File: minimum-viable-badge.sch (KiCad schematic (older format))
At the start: 33 parts, among them J101 EDGE_CONNECTOR, P101 USB, P102 BATTERY, P103 POT_LONG, P104 BUTTON_A, P105 BUTTON_B, P106 POT_SHORT, P107 MECH, P108 MECH, P109 MECH, Q101 S8050, Q102 S8050, SW101 PRGM, SW102 RESET, U101 ESP32-WROOM, U102 CP2102

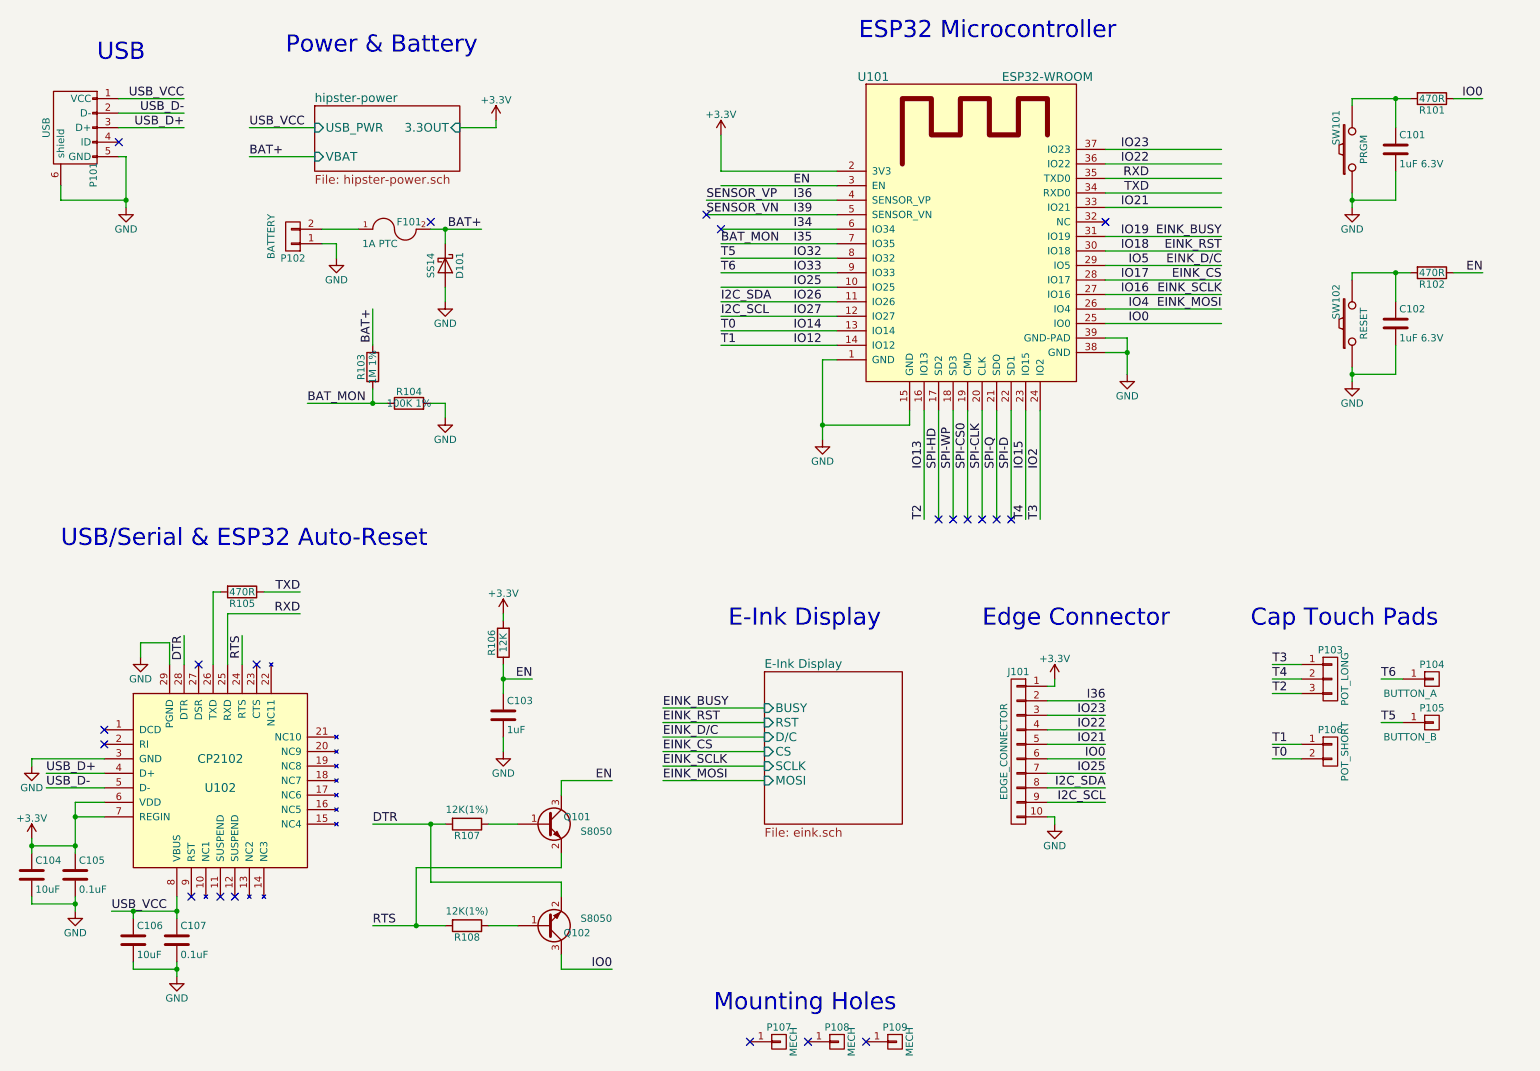
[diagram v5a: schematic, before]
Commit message: Add WS2812Bs for Blinkenlights
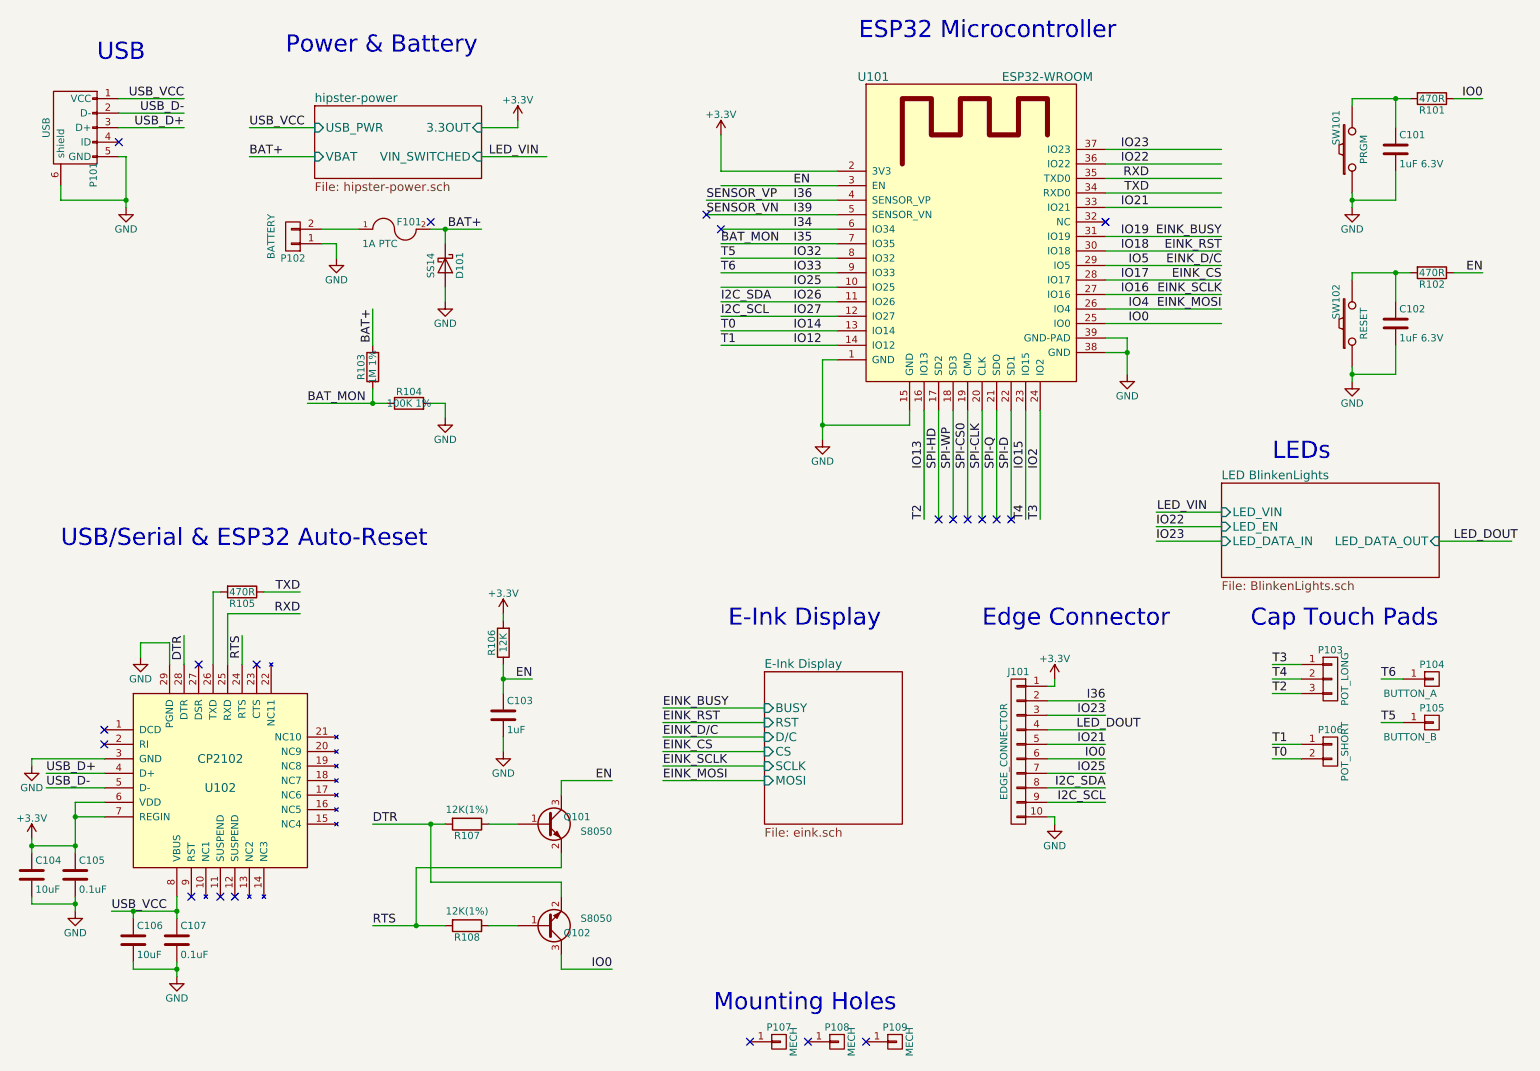
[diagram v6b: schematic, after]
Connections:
- net labels added: LED_DOUT, LED_VIN
- wire segments 149 -> 154
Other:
- note added: "LEDs"
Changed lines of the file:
@@
 $Descr A4 11693 8268
 encoding utf-8
-Sheet 1 3
+Sheet 1 4
 Title ""
 Date ""
@@
 BAT+
 $Sheet
-S 2800 1200 1000 450
+S 2800 1200 1150 500
 U 592826E7
 F0 "hipster-power" 60
@@
 F2 "USB_PWR" I L 2800 1350 60
 F3 "VBAT" I L 2800 1550 60
-F4 "3.3OUT" I R 3800 1350 60
+F4 "3.3OUT" I R 3950 1350 60
+F5 "VIN_SWITCHED" I R 3950 1550 60
 $EndSheet
 $Comp
 L +3.3V #PWR016
 U 1 1 59288975
-P 4050 1300
-F 0 "#PWR016" H 4050 1150 50  0001 C CNN
-F 1 "+3.3V" H 4050 1440 50  0000 C CNN
-F 2 "" H 4050 1300 50  0000 C CNN
-F 3 "" H 4050 1300 50  0000 C CNN
-	1    4050 1300
+P 4200 1300
+F 0 "#PWR016" H 4200 1150 50  0001 C CNN
+F 1 "+3.3V" H 4200 1440 50  0000 C CNN
+F 2 "" H 4200 1300 50  0000 C CNN
+F 3 "" H 4200 1300 50  0000 C CNN
+	1    4200 1300
 	1    0    0    -1
 $EndComp
@@
 Connection ~ 3700 2050
 Wire Wire Line
-	3800 1350 4050 1350
-Wire Wire Line
-	4050 1350 4050 1300
+	3950 1350 4200 1350
+Wire Wire Line
+	4200 1350 4200 1300
 Wire Wire Line
 	2800 1550 2350 1550
@@
 Text Label 8250 5700 2    60   ~ 0
 IO0
-Text Label 8250 5500 2    60   ~ 0
-IO22
-Text Label 8250 5400 2    60   ~ 0
-IO23
 Text Label 8550 1900 2    60   ~ 0
 IO21
 NoConn ~ 5500 1950
 NoConn ~ 5600 2050
+$Sheet
+S 9050 3800 1500 650
+U 59C74472
+F0 "LED BlinkenLights" 60
+F1 "BlinkenLights.sch" 60
+F2 "LED_DATA_IN" I L 9050 4200 60
+F3 "LED_EN" I L 9050 4100 60
+F4 "LED_VIN" I L 9050 4000 60
+F5 "LED_DATA_OUT" I R 10550 4200 60
+$EndSheet
+Text Notes 9400 3650 0    118  ~ 0
+LEDs
+Wire Wire Line
+	10550 4200 11050 4200
+Text Label 10650 4200 0    60   ~ 0
+LED_DOUT
+Text Label 8050 5500 0    60   ~ 0
+LED_DOUT
+Wire Wire Line
+	3950 1550 4400 1550
+Text Label 4000 1550 0    60   ~ 0
+LED_VIN
+Text Label 8950 4000 2    60   ~ 0
+LED_VIN
+Wire Wire Line
+	9050 4000 8600 4000
+Wire Wire Line
+	9050 4100 8600 4100
+Wire Wire Line
+	9050 4200 8600 4200
+Text Label 8600 4100 0    60   ~ 0
+IO22
+Text Label 8600 4200 0    60   ~ 0
+IO23
+Text Label 8250 5400 2    60   ~ 0
+IO23
 $EndSCHEMATC

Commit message: Route LEDs, make edge connector one sided with mounting slots
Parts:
- J101: footprint libs:Edge_Connector_1x10_Pitch2.54mm -> libs:Edge_Connector_S20-2.54-5_bottomsideonly
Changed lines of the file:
@@
 F 0 "J101" H 7650 6200 50  0000 C CNN
 F 1 "EDGE_CONNECTOR" V 7750 5650 50  0000 C CNN
-F 2 "libs:Edge_Connector_1x10_Pitch2.54mm" H 7650 5650 50  0001 C CNN
+F 2 "libs:Edge_Connector_S20-2.54-5_bottomsideonly" H 7650 5650 50  0001 C CNN
 F 3 "" H 7650 5650 50  0001 C CNN
 	1    7650 5650
